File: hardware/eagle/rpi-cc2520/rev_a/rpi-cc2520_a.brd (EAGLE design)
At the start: 20.3 x 34 mm, 22 parts, among them P1 MOLEX_73251-135X, U1 CC2520, X1 NX2520SA

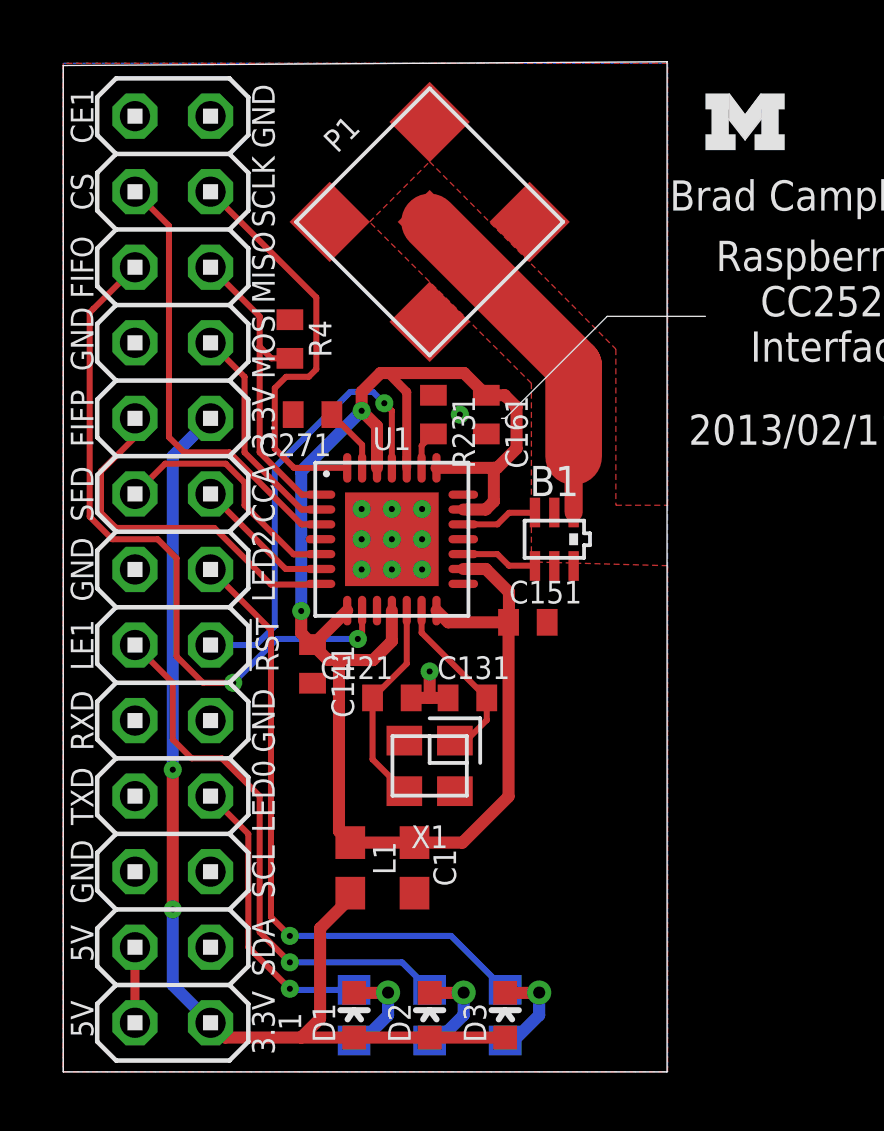
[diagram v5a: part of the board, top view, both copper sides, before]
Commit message: getting the polygons right
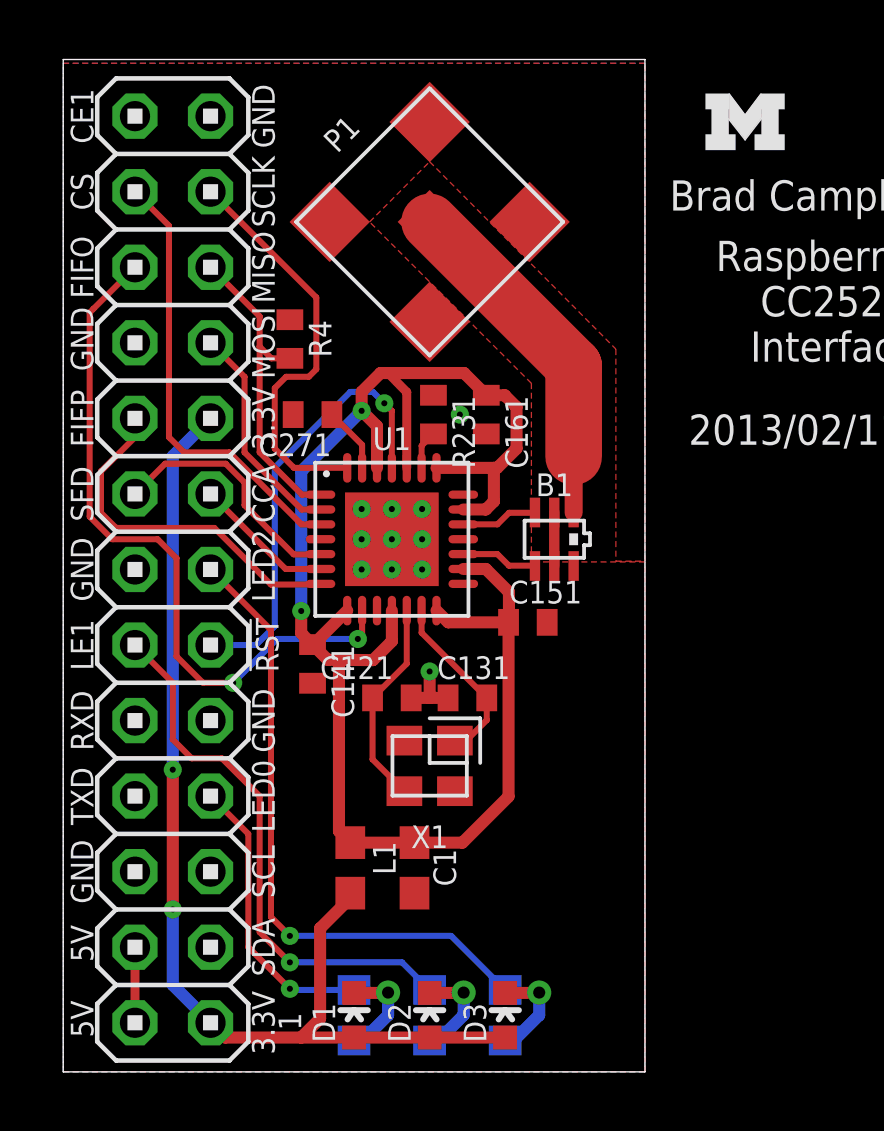
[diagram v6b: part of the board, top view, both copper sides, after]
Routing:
- net GND: track 2.13 -> 3.93 mm
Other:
- board size 20.3 x 34 mm -> 19.6 x 34 mm
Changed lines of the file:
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@@
 <setting verticaltext="up"/>
 </settings>
-<grid distance="1" unitdist="mm" unit="mm" style="lines" multiple="1" display="yes" altdistance="0.1" altunitdist="mm" altunit="mm"/>
+<grid distance="0.1" unitdist="inch" unit="inch" style="lines" multiple="1" display="yes" altdistance="0.05" altunitdist="inch" altunit="inch"/>
 <layers>
 <layer number="1" name="Top" color="4" fill="1" visible="yes" active="yes"/>
@@
 <layer number="49" name="Reference" color="7" fill="1" visible="no" active="yes"/>
 <layer number="50" name="dxf" color="7" fill="1" visible="no" active="no"/>
-<layer number="51" name="tDocu" color="7" fill="1" visible="yes" active="yes"/>
+<layer number="51" name="tDocu" color="7" fill="1" visible="no" active="yes"/>
 <layer number="52" name="bDocu" color="7" fill="1" visible="no" active="yes"/>
 <layer number="53" name="tGND_GNDA" color="7" fill="9" visible="no" active="no"/>
@@
 <board>
 <plain>
-<wire x1="0" y1="0" x2="20.3" y2="0" width="0" layer="20"/>
-<wire x1="20.3" y1="0" x2="20.3" y2="33.96" width="0" layer="20"/>
-<wire x1="20.3" y1="33.96" x2="0" y2="33.833" width="0" layer="20"/>
-<wire x1="0" y1="33.833" x2="0" y2="0" width="0" layer="20"/>
+<wire x1="0" y1="0" x2="19.558" y2="0" width="0" layer="20"/>
+<wire x1="19.558" y1="0" x2="19.558" y2="34.036" width="0" layer="20"/>
+<wire x1="19.558" y1="34.036" x2="0" y2="34.036" width="0" layer="20"/>
+<wire x1="0" y1="34.036" x2="0" y2="0" width="0" layer="20"/>
 <text x="8.001" y="1.397" size="0.762" layer="21" font="vector" ratio="10" rot="R90">1</text>
 <text x="25.908" y="23.876" size="1.016" layer="21" font="vector" ratio="12" align="bottom-center">Raspberry Pi
@@
 <text x="1.016" y="29.591" size="0.762" layer="21" font="vector" ratio="10" rot="R90" align="bottom-center">CS</text>
 <text x="1.016" y="32.131" size="0.762" layer="21" font="vector" ratio="10" rot="R90" align="bottom-center">CE1</text>
-<wire x1="14.859" y1="21.971" x2="18.288" y2="25.4" width="0" layer="21"/>
-<wire x1="18.288" y1="25.4" x2="21.59" y2="25.4" width="0" layer="21"/>
-<wire x1="14.859" y1="21.971" x2="14.732" y2="21.971" width="0" layer="21"/>
 </plain>
 <attributes>
@@
 </class>
 </classes>
-<designrules name="sunstone-2lyr_v1.0.0.3">
+<designrules name="sunstone-2lyr_v1.0.0.3 *">
 <description language="en">&lt;b&gt;EAGLE Design Rules for *2* Layer Designs (DS)&lt;/b&gt;
 &lt;p&gt;
@@
 <param name="mdViaViaSameLayer" value="8mil"/>
 <param name="mnLayersViaInSmd" value="2"/>
-<param name="mdCopperDimension" value="20mil"/>
+<param name="mdCopperDimension" value="10mil"/>
 <param name="mdDrill" value="16mil"/>
 <param name="mdSmdStop" value="0mil"/>
@@
 <attribute name="VALUE" x="5.715" y="25.273" size="1.27" layer="27" rot="R270"/>
 </element>
-<element name="B1" library="rpi-cc2520" package="2450BM" value="2450BM15A0002" x="16.51" y="17.907">
+<element name="B1" library="rpi-cc2520" package="2450BM" value="2450BM15A0002" x="16.51" y="17.907" smashed="yes">
 <attribute name="DIGIKEY" value="712-1536-1-ND" x="16.51" y="17.907" size="0.762" layer="27" font="vector" ratio="10" display="off"/>
+<attribute name="NAME" x="16.51" y="19.357" size="0.762" layer="25" font="vector" ratio="10" align="bottom-center"/>
+<attribute name="VALUE" x="16.51" y="15.457" size="1.016" layer="27" font="vector" ratio="12" align="bottom-center"/>
 </element>
 </elements>
@@
 <polygon width="0.254" layer="16" isolate="0.3048">
 <vertex x="0" y="33.909"/>
-<vertex x="20.32" y="33.909"/>
-<vertex x="20.32" y="0"/>
+<vertex x="19.558" y="33.909"/>
+<vertex x="19.558" y="0"/>
 <vertex x="0" y="0"/>
 </polygon>
@@
 <via x="10.033" y="16.891" extent="1-16" drill="0.2032"/>
 <via x="10.033" y="17.907" extent="1-16" drill="0.2032"/>
-<polygon width="0.2032" layer="1">
+<polygon width="0.2032" layer="1" spacing="0.0254">
 <vertex x="0" y="0"/>
-<vertex x="20.32" y="0"/>
-<vertex x="20.32" y="17.018"/>
+<vertex x="19.558" y="0"/>
+<vertex x="19.558" y="17.145"/>
 <vertex x="15.74" y="17.145"/>
 <vertex x="15.74" y="23.15"/>
@@
 <vertex x="12.319" y="30.6"/>
 <vertex x="18.58" y="24.3"/>
-<vertex x="18.58" y="19.05"/>
-<vertex x="20.32" y="19.05"/>
-<vertex x="20.32" y="33.909"/>
+<vertex x="18.58" y="17.1704"/>
+<vertex x="19.558" y="17.1704"/>
+<vertex x="19.558" y="33.909"/>
 <vertex x="0" y="33.909"/>
 </polygon>
@@
 <contactref element="B1" pad="2"/>
 <contactref element="B1" pad="6"/>
-<wire x1="16.51" y1="17.007" x2="16.51" y2="18.807" width="0" layer="19" extent="1-1"/>
+<wire x1="16.51" y1="18.807" x2="16.51" y2="17.007" width="0.35" layer="1"/>
 </signal>
 <signal name="!RESET">

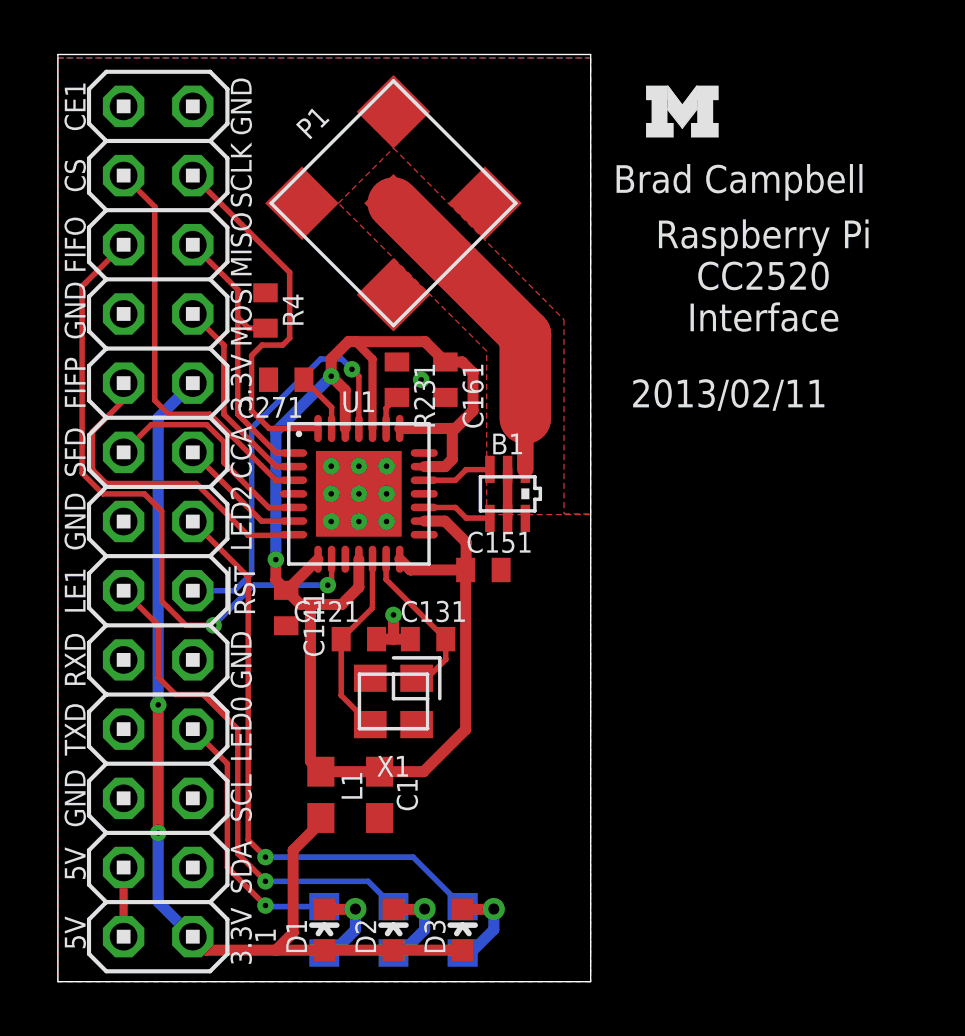
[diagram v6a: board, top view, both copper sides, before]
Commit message: added a ton of vias
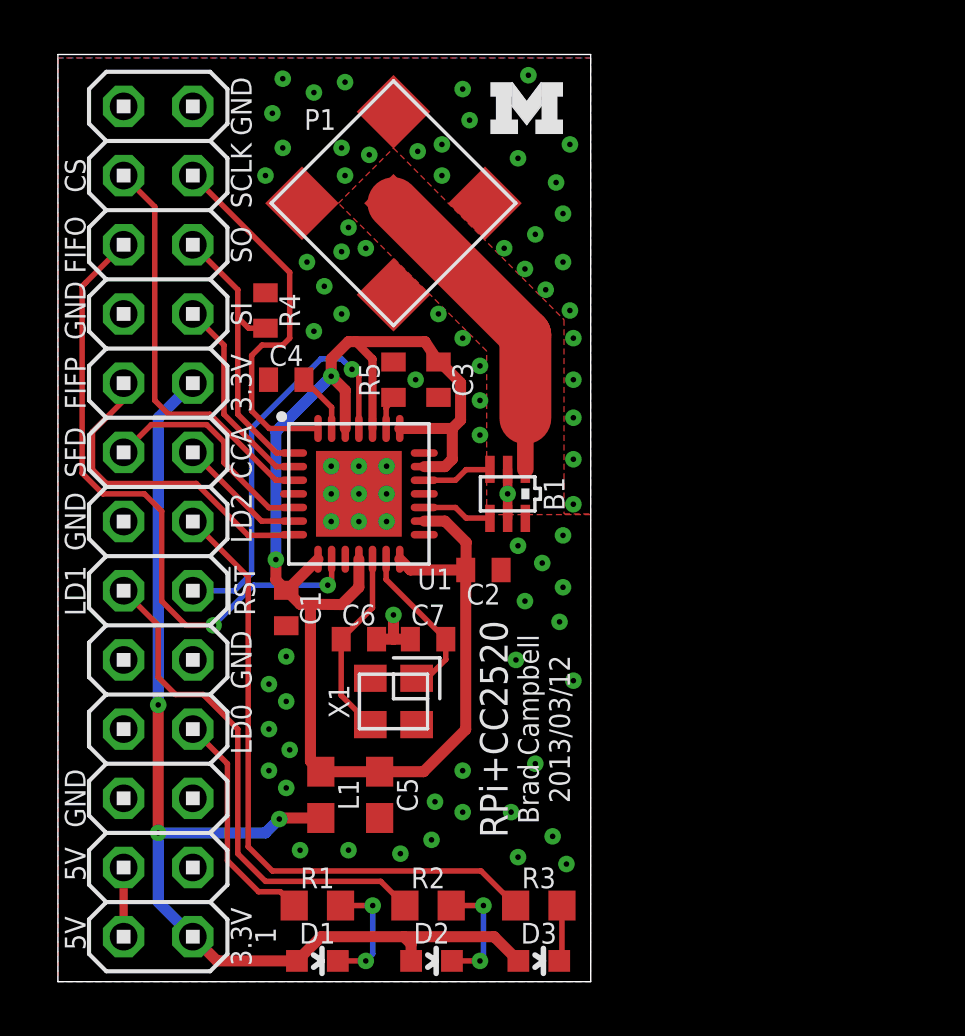
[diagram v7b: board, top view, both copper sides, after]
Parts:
- removed C141, C161: 100nF, rcl:C0402
- removed R231: 56k 1%, rcl:R0402
- added C3: 100nF, rcl:C0402
- added C5: 1uF, rcl:C0603
- added R5: 56k 1%, rcl:R0402
- C1: value 1uF -> 100nF; device rcl:C0603 -> rcl:C0402
- moved C1 7.67 mm to (8.38, 13.7)
- moved U$1 5.72 mm to (15.9, 31.1)
- moved D3 3.02 mm to (17.7, 0.76), turned to 270 degrees
- moved R3 2.93 mm to (17.7, 2.79), flipped to the top, turned to 0 degrees
- moved D2 1.81 mm to (13.7, 0.76), turned to 270 degrees
- moved R2 1.55 mm to (13.6, 2.79), flipped to the top, turned to 0 degrees
- moved D1 1.17 mm to (9.53, 0.76), turned to 270 degrees
- moved R1 0.92 mm to (9.53, 2.79), flipped to the top, turned to 0 degrees
- renumbered C121 to C6, C131 to C7, C151 to C2, C271 to C4, JP2 to J1
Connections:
- net GND: now also C3.2, C5.2, R5.1; no longer C141.2, C161.2, R231.1
- net N$14: now also R5.2; no longer R231.2
- net N$5: now also C3.1, C5.1; no longer C141.1, C161.1
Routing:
- net VCC: track 37.0 -> 41.8 mm, vias 2 -> 3
- net LED2: track 21.4 -> 23.5 mm, vias 1 -> 0
- net N$3: track 3.42 -> 2.07 mm, vias 1 -> 0
- net LED0: track 9.76 -> 8.49 mm, vias 1 -> 0
- net N$1: track 3.42 -> 4.35 mm, vias 1 -> 2
- net N$2: track 3.42 -> 4.29 mm, vias 1 -> 2
- net N$5: track 57.0 -> 56.3 mm
- net LED1: track 18.5 -> 18.9 mm, vias 1 -> 0
- net GND: vias 11 -> 81
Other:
- board text added: "2013/03/12"
- board text added: "LD0"
- board text added: "LD1"
- board text added: "LD2"
- board text added: "RPi+CC2520"
- board text added: "SI"
- board text added: "SO"
- board text removed: "2013/02/11"
- board text removed: "LE1"
- board text removed: "LED0"
- board text removed: "LED2"
- board text removed: "MISO"
- board text removed: "MOSI"
- board text removed: "Raspberry Pi CC2520 Interface"
